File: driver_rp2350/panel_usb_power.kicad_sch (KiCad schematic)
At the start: 4 parts, among them J5 Conn_01x04, U1 AP2112K-3.3

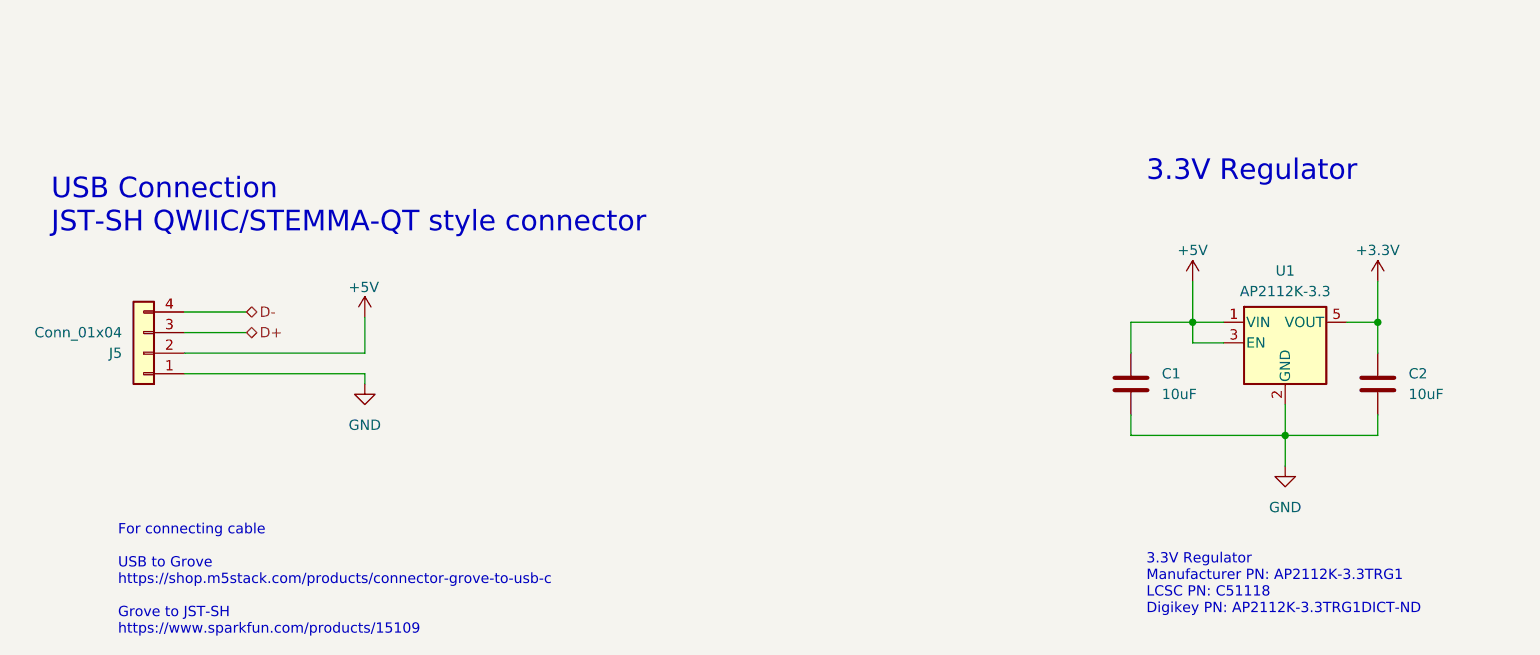
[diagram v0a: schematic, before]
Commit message: Finished first version of schematic for rp2350 G6 panel.
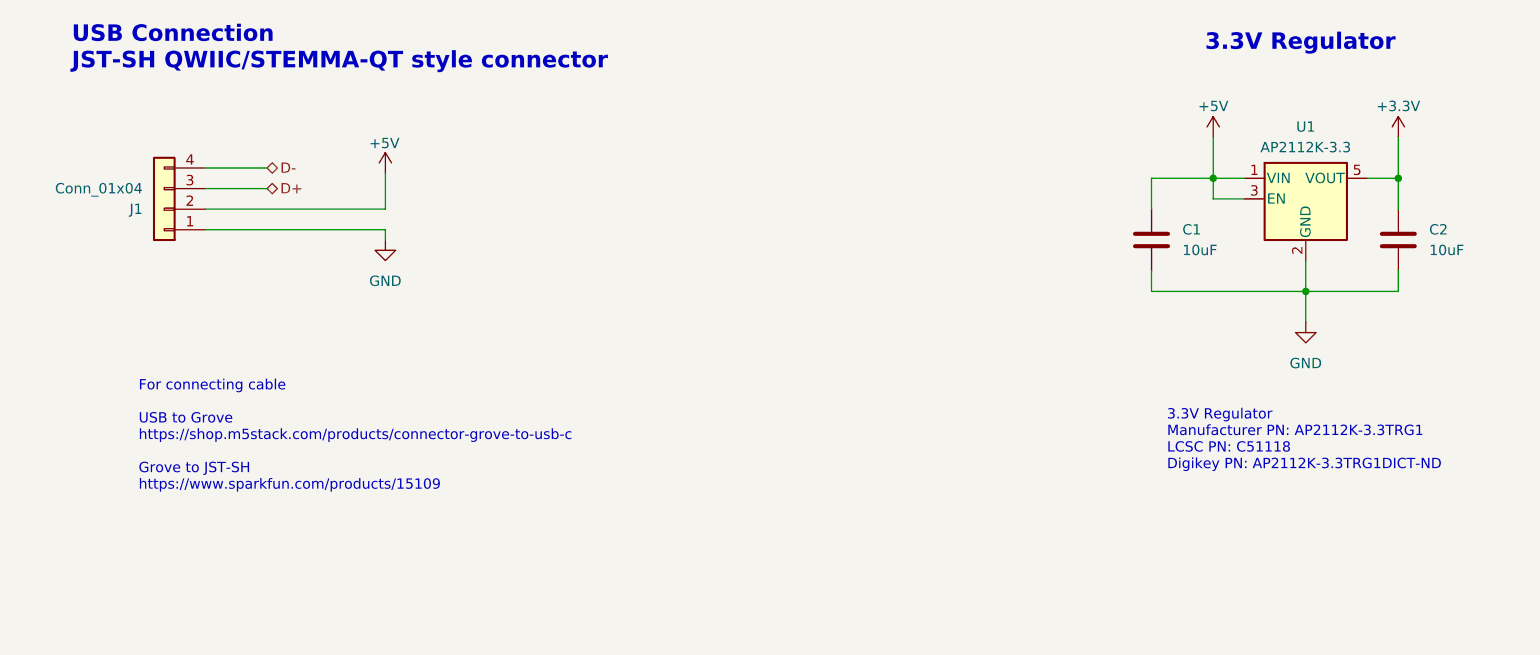
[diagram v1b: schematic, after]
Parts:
- renumbered J5 to J1
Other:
- moved on the sheet: C1, C2, J1, U1
